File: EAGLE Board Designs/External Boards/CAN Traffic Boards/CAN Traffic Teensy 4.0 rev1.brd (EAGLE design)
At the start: 41.6 x 33 mm, 7 parts, among them X1 CONNECTOR-4NANO-FIT_RIGHT_ANG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

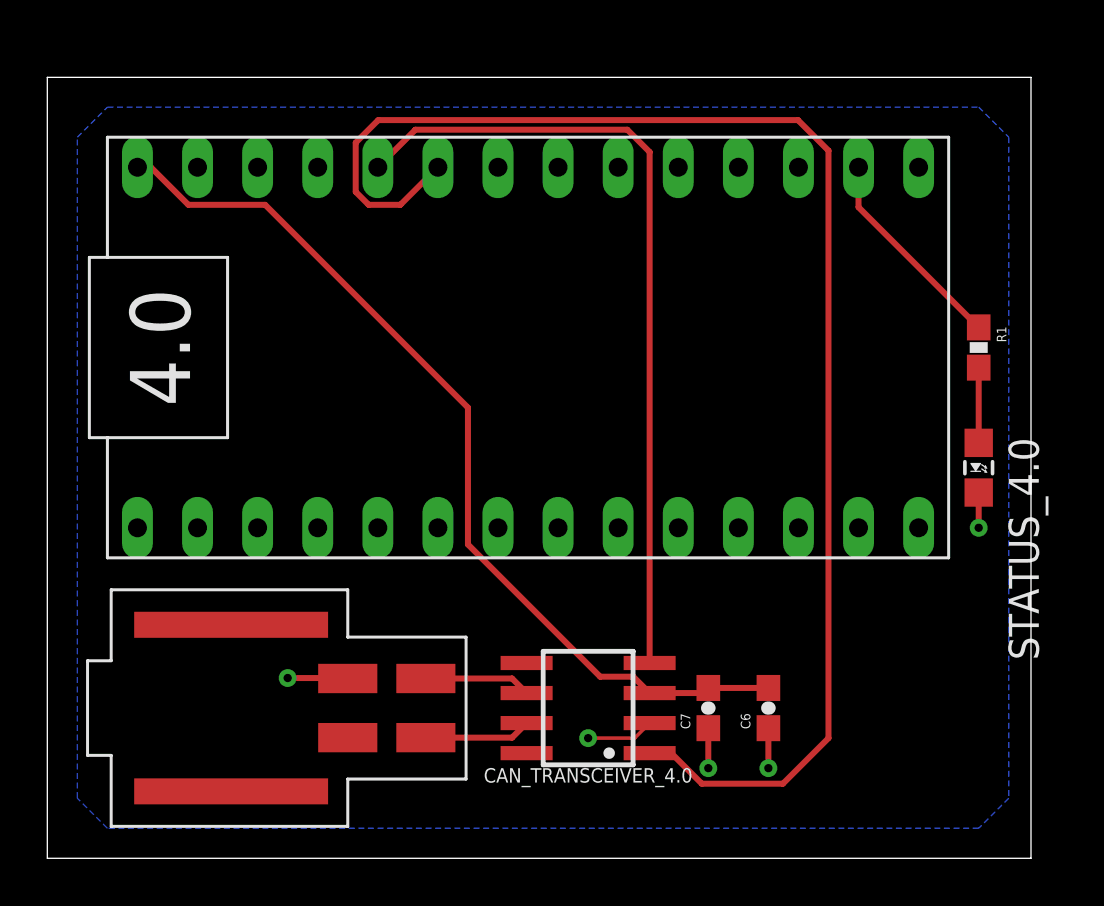
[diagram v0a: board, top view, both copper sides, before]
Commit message: CAN Transceiver Boards
Added CAN Termination resistors, remade boards, added labels, put all LEDs on the same pin, added silksreens, and switched LED packages.
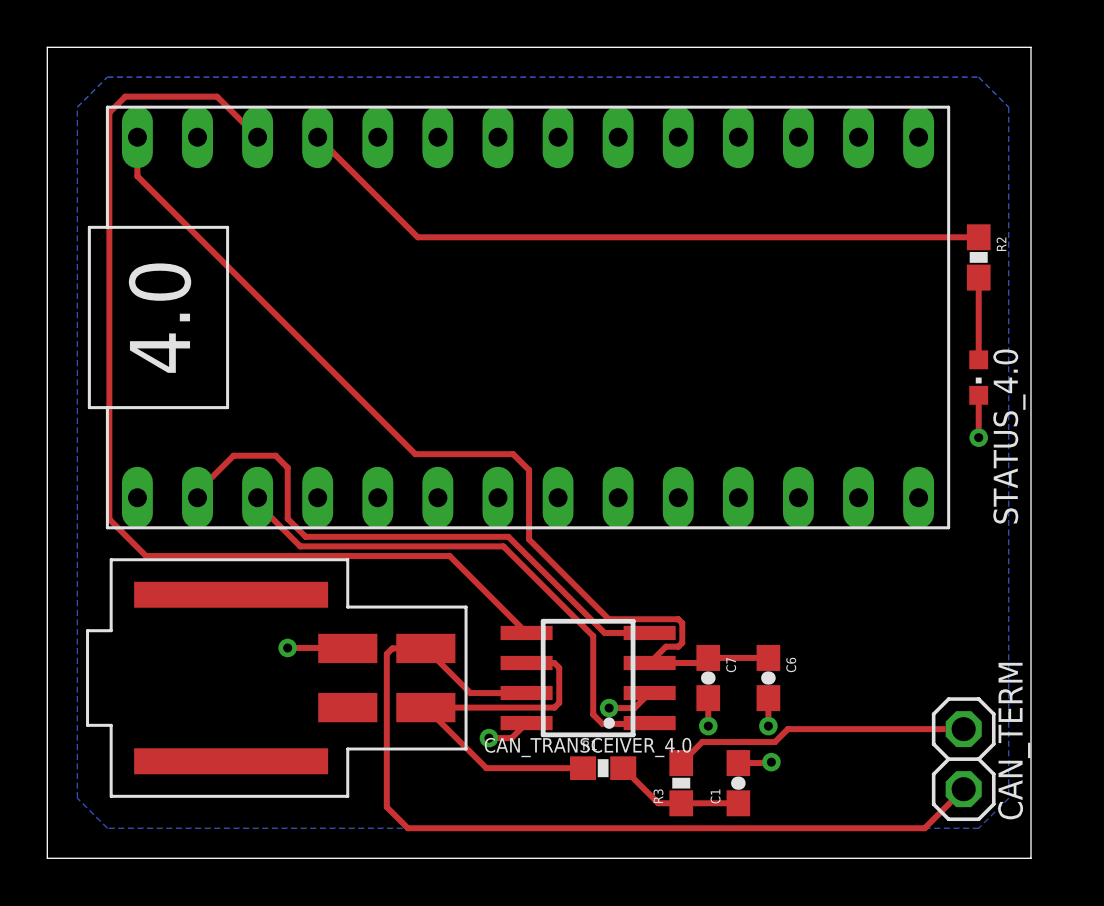
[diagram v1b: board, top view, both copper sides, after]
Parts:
- removed U$2: TEENSY_4.0_SIMPLE, HyTechDevices:TEENSY_4.0_SIMPLE
- added 4.0: TEENSY_4.0_SIMPLE, HyTechDevices:TEENSY_4.0_SIMPLE
- added C1: 4.7nF, HyTechDevices:0603-CAP
- added CAN_TERM: M02_SLIM, HyTechDevices:1X02_SLIM
- added R2: 1k, HyTechDevices:0603-RES
- added R3: 60, HyTechDevices:0603-RES
- CAN_TRANSCEIVER_4.0: value MCP2562SOIC-08 -> MCP2562FDSOIC-08
- R1: value 1k -> 60
- STATUS_4.0: device HyTechDevices:LED-805 -> HyTechDevices:LED-603
- moved R1 23.8 mm to (23.5, 3.81), turned to 0 degrees
- moved STATUS_4.0 3.81 mm to (39.4, 20.3)
- moved C6 1.27 mm to (30.5, 7.62), turned to 270 degrees
- moved C7 1.27 mm to (27.9, 7.62), turned to 270 degrees
- moved CAN_TRANSCEIVER_4.0 1.27 mm to (22.9, 7.62)
- moved X1 1.27 mm to (12.7, 7.62)
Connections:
- removed net N$3: CAN_TRANSCEIVER_4.0.4, U$2.(CANRX)A8
- removed net N$6: CAN_TRANSCEIVER_4.0.5
- new net +3V3: 4.0.3.3V, CAN_TRANSCEIVER_4.0.5
- new net CANRX: 4.0.D0(RX1), CAN_TRANSCEIVER_4.0.4
- new net CANTX: 4.0.D1(TX1), CAN_TRANSCEIVER_4.0.1
- net +5V: now also 4.0.VIN, C6.1, C7.1; no longer C6.2, C7.2, U$2.VIN
- net CANH: now also CAN_TERM.1, CAN_TRANSCEIVER_4.0.7; no longer CAN_TRANSCEIVER_4.0.6
- net CANL: now also CAN_TRANSCEIVER_4.0.6, R1.1; no longer CAN_TRANSCEIVER_4.0.7
- net GND: now also 4.0.GND, C1.2, C6.2, C7.2, CAN_TRANSCEIVER_4.0.8; no longer C6.1, C7.1, U$2.GND
- net N$1: now also 4.0.A9, R2.1; no longer R1.2, STATUS_4.0.A
- net N$2: now also R2.2, STATUS_4.0.A; no longer R1.1, U$2.(TX3)A0
- net N$4: now also C1.1, R1.2, R3.1; no longer CAN_TRANSCEIVER_4.0.1, U$2.(CANTX)A7
- net N$5: now also CAN_TERM.2, R3.2; no longer CAN_TRANSCEIVER_4.0.8
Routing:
- net N$4: track 61.1 -> 5.48 mm
- net +3V3: track 0.00 -> 44.1 mm
- net CANH: track 4.51 -> 38.7 mm
- net N$3: track 34.1 -> 0.00 mm
- net N$1: track 3.18 -> 29.7 mm
- net CANRX: track 0.00 -> 24.4 mm
- net CANTX: track 0.00 -> 22.6 mm
- net N$5: track 0.00 -> 12.5 mm
- net CANL: track 4.51 -> 16.4 mm
- net N$2: track 8.87 -> 3.48 mm
- net +5V: track 39.4 -> 41.9 mm
- net GND: track 10.3 -> 11.9 mm, vias 5 -> 7
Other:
- board size 41.6 x 33 mm -> 41.6 x 34.3 mm
- board text added: "TEENSY 4.0"

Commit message: small changes for JLC DRC
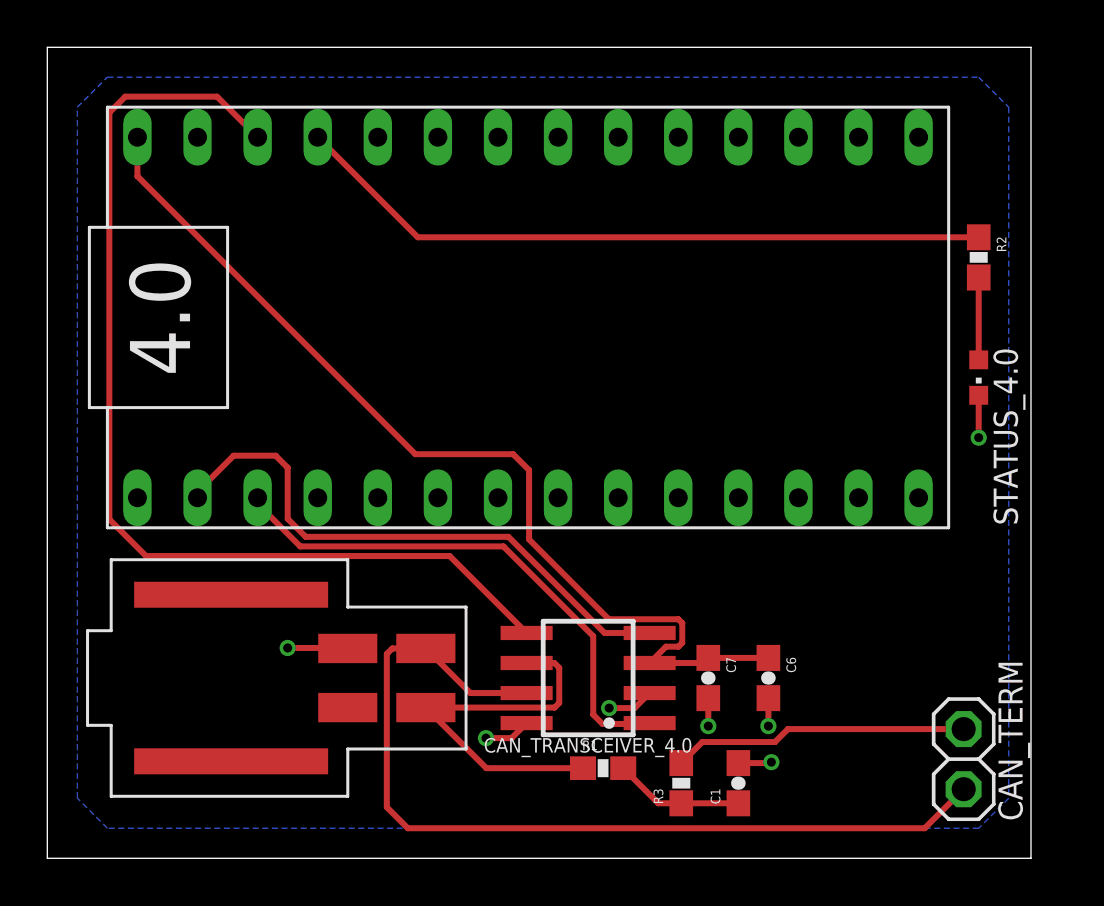
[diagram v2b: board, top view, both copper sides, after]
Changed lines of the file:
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@@
 </class>
 </classes>
-<designrules name="default">
-<description language="de">&lt;b&gt;EAGLE Design Rules&lt;/b&gt;
-&lt;p&gt;
-Die Standard-Design-Rules sind so gewählt, dass sie für
-die meisten Anwendungen passen. Sollte ihre Platine
-besondere Anforderungen haben, treffen Sie die erforderlichen
-Einstellungen hier und speichern die Design Rules unter
-einem neuen Namen ab.</description>
-<description language="en">&lt;b&gt;EAGLE Design Rules&lt;/b&gt;
+<designrules name="JLCPCB (2 Layer)">
+<description language="en">&lt;b&gt;JLCPCB Design Rules (2 Layers)&lt;/b&gt;
 &lt;p&gt;
 The default Design Rules have been set to cover
-a wide range of applications. Your particular design
-may have different requirements, so please make the
-necessary adjustments and save your customized
-design rules under a new name.</description>
+a wide range of applications.
+&lt;p&gt;
+Source: &lt;a href=&quot;https://jlcpcb.com/capabilities/Capabilities&quot;&gt;JLCPCB&lt;/a&gt;
+&lt;/p&gt;</description>
 <param name="layerSetup" value="(1*16)"/>
 <param name="mtCopper" value="0.035mm 0.035mm 0.035mm 0.035mm 0.035mm 0.035mm 0.035mm 0.035mm 0.035mm 0.035mm 0.035mm 0.035mm 0.035mm 0.035mm 0.035mm 0.035mm"/>
-<param name="mtIsolate" value="1.5mm 0.15mm 0.2mm 0.15mm 0.2mm 0.15mm 0.2mm 0.15mm 0.2mm 0.15mm 0.2mm 0.15mm 0.2mm 0.15mm 0.2mm"/>
-<param name="mdWireWire" value="6mil"/>
-<param name="mdWirePad" value="6mil"/>
-<param name="mdWireVia" value="6mil"/>
-<param name="mdPadPad" value="6mil"/>
-<param name="mdPadVia" value="6mil"/>
-<param name="mdViaVia" value="6mil"/>
-<param name="mdSmdPad" value="6mil"/>
-<param name="mdSmdVia" value="6mil"/>
-<param name="mdSmdSmd" value="6mil"/>
+<param name="mtIsolate" value="1.53mm 0.15mm 0.2mm 0.15mm 0.2mm 0.15mm 0.2mm 0.15mm 0.2mm 0.15mm 0.2mm 0.15mm 0.2mm 0.15mm 0.2mm"/>
+<param name="mdWireWire" value="5mil"/>
+<param name="mdWirePad" value="5mil"/>
+<param name="mdWireVia" value="8mil"/>
+<param name="mdPadPad" value="5mil"/>
+<param name="mdPadVia" value="10mil"/>
+<param name="mdViaVia" value="20mil"/>
+<param name="mdSmdPad" value="5mil"/>
+<param name="mdSmdVia" value="10mil"/>
+<param name="mdSmdSmd" value="5mil"/>
 <param name="mdViaViaSameLayer" value="6mil"/>
 <param name="mnLayersViaInSmd" value="2"/>
-<param name="mdCopperDimension" value="40mil"/>
-<param name="mdDrill" value="6mil"/>
+<param name="mdCopperDimension" value="0.2mm"/>
+<param name="mdDrill" value="21mil"/>
 <param name="mdSmdStop" value="0mil"/>
-<param name="msWidth" value="6mil"/>
-<param name="msDrill" value="0.35mm"/>
+<param name="msWidth" value="5mil"/>
+<param name="msDrill" value="0.3mm"/>
 <param name="msMicroVia" value="9.99mm"/>
 <param name="msBlindViaRatio" value="0.5"/>
@@
 <param name="rvViaOuter" value="0.25"/>
 <param name="rvViaInner" value="0.25"/>
-<param name="rvMicroViaOuter" value="0.25"/>
-<param name="rvMicroViaInner" value="0.25"/>
-<param name="rlMinPadTop" value="10mil"/>
+<param name="rvMicroViaOuter" value="0"/>
+<param name="rvMicroViaInner" value="0"/>
+<param name="rlMinPadTop" value="6mil"/>
 <param name="rlMaxPadTop" value="20mil"/>
-<param name="rlMinPadInner" value="10mil"/>
+<param name="rlMinPadInner" value="6mil"/>
 <param name="rlMaxPadInner" value="20mil"/>
-<param name="rlMinPadBottom" value="10mil"/>
+<param name="rlMinPadBottom" value="6mil"/>
 <param name="rlMaxPadBottom" value="20mil"/>
-<param name="rlMinViaOuter" value="8mil"/>
-<param name="rlMaxViaOuter" value="20mil"/>
-<param name="rlMinViaInner" value="8mil"/>
-<param name="rlMaxViaInner" value="20mil"/>
-<param name="rlMinMicroViaOuter" value="4mil"/>
+<param name="rlMinViaOuter" value="6mil"/>
+<param name="rlMaxViaOuter" value="12mil"/>
+<param name="rlMinViaInner" value="6mil"/>
+<param name="rlMaxViaInner" value="12mil"/>
+<param name="rlMinMicroViaOuter" value="6mil"/>
 <param name="rlMaxMicroViaOuter" value="20mil"/>
-<param name="rlMinMicroViaInner" value="4mil"/>
+<param name="rlMinMicroViaInner" value="6mil"/>
 <param name="rlMaxMicroViaInner" value="20mil"/>
 <param name="psTop" value="-1"/>
 <param name="psBottom" value="-1"/>
-<param name="psFirst" value="-1"/>
+<param name="psFirst" value="0"/>
 <param name="psElongationLong" value="100"/>
 <param name="psElongationOffset" value="100"/>
 <param name="mvStopFrame" value="1"/>
 <param name="mvCreamFrame" value="0"/>
-<param name="mlMinStopFrame" value="4mil"/>
-<param name="mlMaxStopFrame" value="4mil"/>
+<param name="mlMinStopFrame" value="6mil"/>
+<param name="mlMaxStopFrame" value="6mil"/>
 <param name="mlMinCreamFrame" value="0mil"/>
 <param name="mlMaxCreamFrame" value="0mil"/>
-<param name="mlViaStopLimit" value="0mil"/>
+<param name="mlViaStopLimit" value="30mil"/>
 <param name="srRoundness" value="0"/>
 <param name="srMinRoundness" value="0mil"/>
@@
 <param name="checkRestrict" value="1"/>
 <param name="checkStop" value="0"/>
-<param name="checkValues" value="0"/>
+<param name="checkValues" value="1"/>
 <param name="checkNames" value="1"/>
 <param name="checkWireStubs" value="1"/>
-<param name="checkPolygonWidth" value="0"/>
+<param name="checkPolygonWidth" value="1"/>
 <param name="useDiameter" value="13"/>
 <param name="maxErrors" value="50"/>
@@
 </polygon>
 <wire x1="20.26" y1="5.715" x2="19.625" y2="5.08" width="0.254" layer="1"/>
-<wire x1="19.625" y1="5.08" x2="18.669" y2="5.08" width="0.254" layer="1"/>
-<via x="18.669" y="5.08" extent="1-16" drill="0.381"/>
+<wire x1="19.625" y1="5.08" x2="18.542" y2="5.08" width="0.254" layer="1"/>
+<via x="18.542" y="5.08" extent="1-16" drill="0.381"/>
 <wire x1="12.7" y1="8.87" x2="12.68" y2="8.89" width="0.254" layer="1"/>
 <wire x1="12.68" y1="8.89" x2="10.16" y2="8.89" width="0.254" layer="1"/>
